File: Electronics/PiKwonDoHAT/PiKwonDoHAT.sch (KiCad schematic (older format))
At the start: 5 parts

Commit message: Finished HAT schematic
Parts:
- J1: renamed from J?; footprint (none) -> Pin_Headers:Pin_Header_Straight_2x20_Pitch2.54mm
- J2: renamed from J?; value RJ12-UNSHLD -> Judge3; footprint (none) -> PiKwonDo:TH-RJ12
- J3: renamed from J?; value RJ12-UNSHLD -> Judge2; footprint (none) -> PiKwonDo:TH-RJ12
- J4: renamed from J?; value RJ12-UNSHLD -> Judge1; footprint (none) -> PiKwonDo:TH-RJ12
- J5: renamed from J?; value RJ12-UNSHLD -> Controller; footprint (none) -> PiKwonDo:TH-RJ12
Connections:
- net labels added: CLK, LOAD
- net labels removed: VCC
- wire segments 0 -> 24
- no-connect marks 0 -> 41
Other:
- moved on the sheet: J1, J2, J3, J4, J5

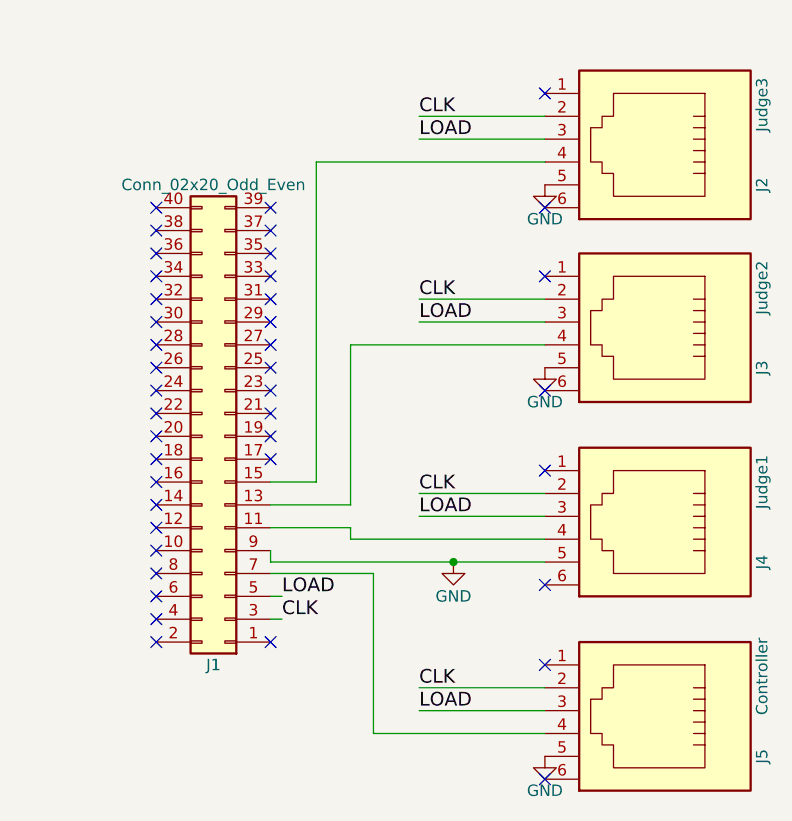
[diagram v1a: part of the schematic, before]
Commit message: Created HAT schematic and PCB
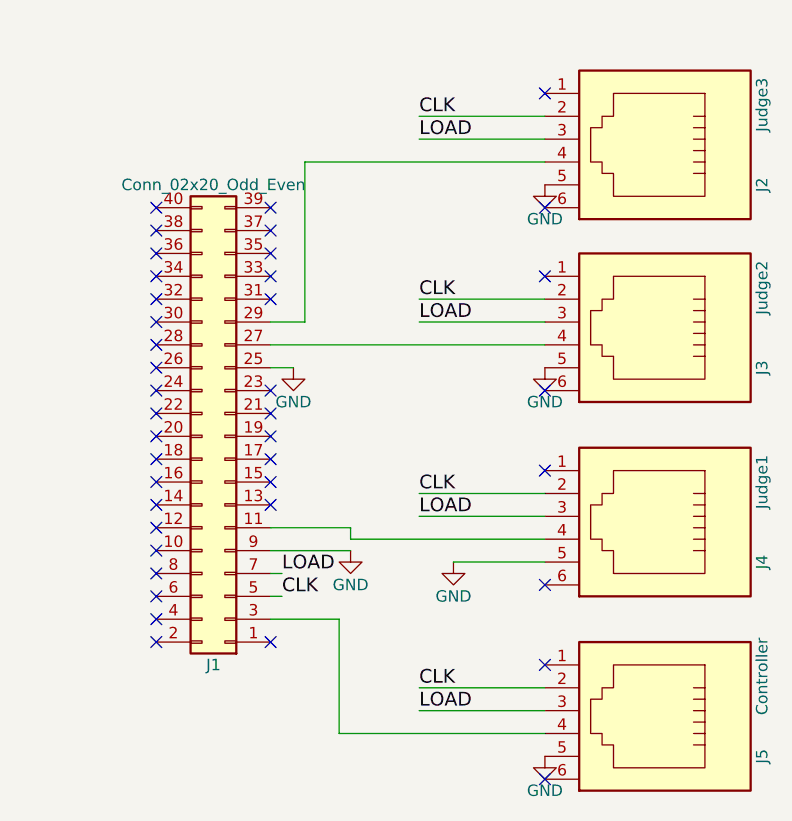
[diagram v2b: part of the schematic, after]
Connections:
- net CLK: now also J1.5 (Pin_5); no longer J1.3 (Pin_3)
- net GND: now also J1.25 (Pin_25)
- net LOAD: now also J1.7 (Pin_7); no longer J1.5 (Pin_5)
- net at J2.4: now also J1.29 (Pin_29); no longer J1.15 (Pin_15)
- net at J3.4: now also J1.27 (Pin_27); no longer J1.13 (Pin_13)
- net at J5.4: now also J1.3 (Pin_3); no longer J1.7 (Pin_7)
- no-connect marks 41 -> 40
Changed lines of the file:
@@
 LOAD
 Wire Wire Line
-	5800 3400 5850 3400
+	5800 3400 6100 3400
 Wire Wire Line
 	5800 3300 5850 3300
-Text Label 5850 3400 0    60   ~ 0
+Text Label 5850 3300 0    60   ~ 0
 CLK
-Text Label 5850 3300 0    60   ~ 0
+Text Label 5850 3200 0    60   ~ 0
 LOAD
-Wire Wire Line
-	7000 3900 6250 3900
-Wire Wire Line
-	6250 3900 6250 3200
-Wire Wire Line
-	6250 3200 5800 3200
 Wire Wire Line
 	7000 3050 6150 3050
@@
 	6150 3050 6150 3000
 Wire Wire Line
-	6150 3000 5800 3000
-Wire Wire Line
-	7000 2200 6150 2200
-Wire Wire Line
-	6150 2200 6150 2900
-Wire Wire Line
-	6150 2900 5800 2900
-Wire Wire Line
-	7000 1400 6000 1400
-Wire Wire Line
-	6000 1400 6000 2800
-Wire Wire Line
-	6000 2800 5800 2800
-Wire Wire Line
-	5800 3150 5800 3100
-Wire Wire Line
-	5800 3150 7000 3150
-Connection ~ 6600 3150
+	6600 3150 7000 3150
 NoConn ~ 5300 3500
 NoConn ~ 5300 3400
@@
 NoConn ~ 5300 1700
 NoConn ~ 5300 1600
-NoConn ~ 5800 3500
 NoConn ~ 5800 2700
 NoConn ~ 5800 2600
 NoConn ~ 5800 2500
 NoConn ~ 5800 2400
-NoConn ~ 5800 2300
-NoConn ~ 5800 2200
-NoConn ~ 5800 2100
 NoConn ~ 5800 2000
 NoConn ~ 5800 1900
@@
 NoConn ~ 5800 1700
 NoConn ~ 5800 1600
+Wire Wire Line
+	6150 3000 5800 3000
+Wire Wire Line
+	6100 3400 6100 3900
+Wire Wire Line
+	6100 3900 7000 3900
+Wire Wire Line
+	5800 3200 5850 3200
+NoConn ~ 5800 3500
+$Comp
+L GND #PWR07
+U 1 1 5B2B12EF
+P 6150 3100
+F 0 "#PWR07" H 6150 2850 50  0001 C CNN
+F 1 "GND" H 6150 2950 50  0000 C CNN
+F 2 "" H 6150 3100 50  0001 C CNN
+F 3 "" H 6150 3100 50  0001 C CNN
+	1    6150 3100
+	1    0    0    -1
+$EndComp
+Wire Wire Line
+	5800 3100 6150 3100
+$Comp
+L GND #PWR08
+U 1 1 5B2B134C
+P 5900 2300
+F 0 "#PWR08" H 5900 2050 50  0001 C CNN
+F 1 "GND" H 5900 2150 50  0000 C CNN
+F 2 "" H 5900 2300 50  0001 C CNN
+F 3 "" H 5900 2300 50  0001 C CNN
+	1    5900 2300
+	1    0    0    -1
+$EndComp
+Wire Wire Line
+	5800 2300 5900 2300
+NoConn ~ 5800 2800
+Wire Wire Line
+	7000 1400 5950 1400
+Wire Wire Line
+	5950 1400 5950 2100
+Wire Wire Line
+	5950 2100 5800 2100
+Wire Wire Line
+	5800 2200 7000 2200
+NoConn ~ 5800 2900
 $EndSCHEMATC

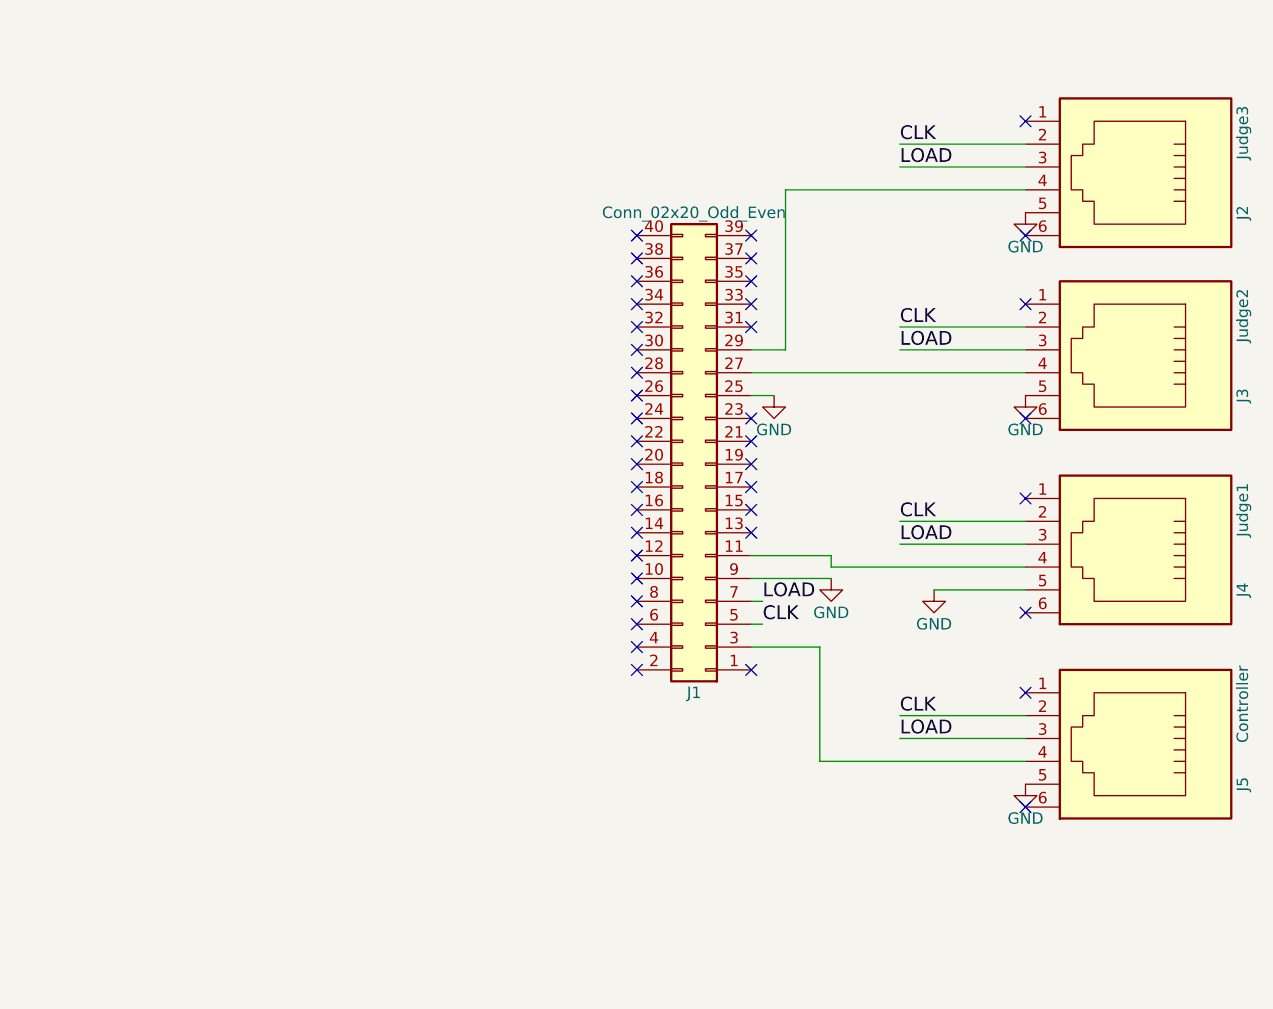
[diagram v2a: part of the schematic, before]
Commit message: Updated circuit protection elements to HAT schematic board.
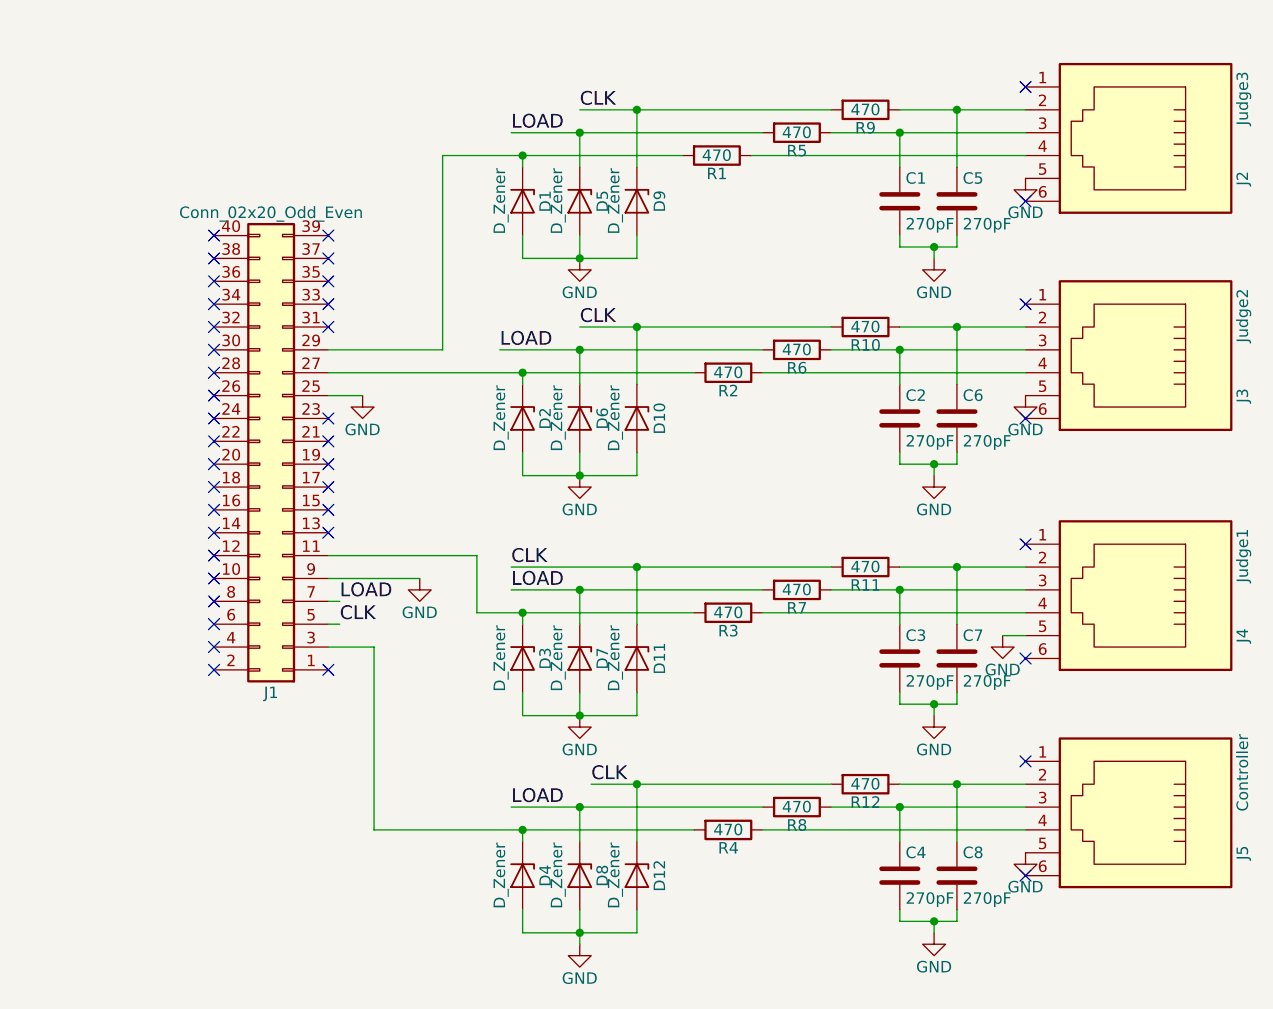
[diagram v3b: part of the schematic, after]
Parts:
- added C1, C2, C3, C4, C5, C6, C7, C8: 270pF, Capacitors_SMD:C_0603_HandSoldering, symbol C
- added D1, D10, D11, D12, D2, D3, D4, D5, D6, D7, D8, D9: D_Zener, Diodes_SMD:SOD-80C, symbol D_Zener
- added R1, R10, R11, R12, R2, R3, R4, R5, R6, R7, R8, R9: 470, Resistors_SMD:R_1206_HandSoldering, symbol R
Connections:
- net CLK: now also D10.1 (K), D11.1 (K), D12.1 (K), D9.1 (K), R10.2, R11.2, R12.2, R9.2; no longer J2.2, J3.2, J4.2, J5.2
- net GND: now also C1.2, C2.2, C3.2, C4.2, C5.2, C6.2, C7.2, C8.2, D1.2 (A), D10.2 (A), D11.2 (A), D12.2 (A), D2.2 (A), D3.2 (A), D4.2 (A), D5.2 (A), D6.2 (A), D7.2 (A), D8.2 (A), D9.2 (A)
- net LOAD: now also D5.1 (K), D6.1 (K), D7.1 (K), D8.1 (K), R5.2, R6.2, R7.2, R8.2; no longer J2.3, J3.3, J4.3, J5.3
- net at J2.4: now also R1.1; no longer J1.29 (Pin_29)
- net at J3.4: now also R2.1; no longer J1.27 (Pin_27)
- net at J4.4: now also R3.1; no longer J1.11 (Pin_11)
- net at J5.4: now also R4.1; no longer J1.3 (Pin_3)
- new net: C5.1, J2.2, R9.1
- new net: C1.1, J2.3, R5.1
- new net: C6.1, J3.2, R10.1
- new net: C2.1, J3.3, R6.1
- new net: C7.1, J4.2, R11.1
- new net: C3.1, J4.3, R7.1
- new net: C8.1, J5.2, R12.1
- new net: C4.1, J5.3, R8.1
- new net: D3.1 (K), J1.11 (Pin_11), R3.2
- new net: D2.1 (K), J1.27 (Pin_27), R2.2
- new net: D1.1 (K), J1.29 (Pin_29), R1.2
- new net: D4.1 (K), J1.3 (Pin_3), R4.2
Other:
- moved on the sheet: J1, J2, J4, J5

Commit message: Updated CAM files for Timer and PCB for HAT
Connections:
- net GND: now also J1.34 (Pin_34), J1.6 (Pin_6)
- no-connect marks 40 -> 38
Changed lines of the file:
@@
 LIBS:contrib
 LIBS:valves
-LIBS:Device
 LIBS:PiKwonDoHAT-cache
 EELAYER 25 0
@@
 NoConn ~ 3450 3500
 NoConn ~ 3450 3400
-NoConn ~ 3450 3300
 NoConn ~ 3450 3200
 NoConn ~ 3450 3100
@@
 NoConn ~ 3450 2100
 NoConn ~ 3450 2000
-NoConn ~ 3450 1900
 NoConn ~ 3450 1800
 NoConn ~ 3450 1700
@@
 Connection ~ 6450 3150
 Wire Wire Line
-	7000 4000 6450 4000
+	6450 4000 7000 4000
 Wire Wire Line
 	7000 4200 5850 4200
@@
 	4800 4250 4800 4200
 Connection ~ 4800 4200
+$Comp
+L GND #PWR?
+U 1 1 5B4F3E4D
+P 3300 3400
+F 0 "#PWR?" H 3300 3150 50  0001 C CNN
+F 1 "GND" H 3300 3250 50  0000 C CNN
+F 2 "" H 3300 3400 50  0001 C CNN
+F 3 "" H 3300 3400 50  0001 C CNN
+	1    3300 3400
+	1    0    0    -1
+$EndComp
+Wire Wire Line
+	3450 3300 3300 3300
+Wire Wire Line
+	3300 3300 3300 3400
+$Comp
+L GND #PWR?
+U 1 1 5B4F406A
+P 3250 2100
+F 0 "#PWR?" H 3250 1850 50  0001 C CNN
+F 1 "GND" H 3250 1950 50  0000 C CNN
+F 2 "" H 3250 2100 50  0001 C CNN
+F 3 "" H 3250 2100 50  0001 C CNN
+	1    3250 2100
+	1    0    0    -1
+$EndComp
+Wire Wire Line
+	3450 1900 3250 1900
+Wire Wire Line
+	3250 1900 3250 2100
 $EndSCHEMATC

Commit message: Finalized HAT PCB
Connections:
- net LOAD: now also J1.8 (Pin_8); no longer J1.7 (Pin_7)
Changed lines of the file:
@@
 LIBS:contrib
 LIBS:valves
+LIBS:Device
 LIBS:PiKwonDoHAT-cache
 EELAYER 25 0
@@
 Text Label 4000 3300 0    60   ~ 0
 CLK
-Text Label 4000 3200 0    60   ~ 0
+Text Label 3050 3200 0    60   ~ 0
 LOAD
 NoConn ~ 3450 3500
 NoConn ~ 3450 3400
-NoConn ~ 3450 3200
 NoConn ~ 3450 3100
 NoConn ~ 3450 3000
@@
 L GND #PWR08
 U 1 1 5B2B134C
-P 4100 2300
-F 0 "#PWR08" H 4100 2050 50  0001 C CNN
-F 1 "GND" H 4100 2150 50  0000 C CNN
-F 2 "" H 4100 2300 50  0001 C CNN
-F 3 "" H 4100 2300 50  0001 C CNN
-	1    4100 2300
+P 4350 2300
+F 0 "#PWR08" H 4350 2050 50  0001 C CNN
+F 1 "GND" H 4350 2150 50  0000 C CNN
+F 2 "" H 4350 2300 50  0001 C CNN
+F 3 "" H 4350 2300 50  0001 C CNN
+	1    4350 2300
 	1    0    0    -1
 $EndComp
@@
 	4150 3400 4150 4200
 Wire Wire Line
-	3950 3200 4000 3200
-Wire Wire Line
 	3950 3100 4350 3100
 Wire Wire Line
-	3950 2300 4100 2300
+	3950 2300 4350 2300
 Wire Wire Line
 	4450 1250 4450 2100
@@
 	4700 2100 5850 2100
 Wire Wire Line
-	3950 2200 5550 2200
-Wire Wire Line
 	5850 2200 7000 2200
 Connection ~ 6450 2100
@@
 Connection ~ 4800 4200
 $Comp
-L GND #PWR?
+L GND #PWR017
 U 1 1 5B4F3E4D
 P 3300 3400
-F 0 "#PWR?" H 3300 3150 50  0001 C CNN
+F 0 "#PWR017" H 3300 3150 50  0001 C CNN
 F 1 "GND" H 3300 3250 50  0000 C CNN
 F 2 "" H 3300 3400 50  0001 C CNN
@@
 	3300 3300 3300 3400
 $Comp
-L GND #PWR?
+L GND #PWR018
 U 1 1 5B4F406A
 P 3250 2100
-F 0 "#PWR?" H 3250 1850 50  0001 C CNN
+F 0 "#PWR018" H 3250 1850 50  0001 C CNN
 F 1 "GND" H 3250 1950 50  0000 C CNN
 F 2 "" H 3250 2100 50  0001 C CNN
@@
 Wire Wire Line
 	3250 1900 3250 2100
+Wire Wire Line
+	3950 2200 5550 2200
+NoConn ~ 3950 3200
+Wire Wire Line
+	3450 3200 3050 3200
 $EndSCHEMATC

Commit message: Added voltage buffer to HAT schematic
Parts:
- added C10, C11, C12, C9: 100pF, Capacitors_SMD:C_0805_HandSoldering, symbol C
- added U1, U2, U3, U4: 74LV1T34, TO_SOT_Packages_SMD:SOT-23-5_HandSoldering, symbol 74LV1T34
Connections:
- net CLK: now also U1.2 (A), U2.2 (A), U3.2 (A), U4.2 (A); no longer D10.1 (K), D11.1 (K), D12.1 (K), D9.1 (K), R10.2, R11.2, R12.2, R9.2
- net GND: now also C10.2, C11.2, C12.2, C9.2, U1.3 (GND), U2.3 (GND), U3.3 (GND), U4.3 (GND)
- net at D3.1 (K), J1.11 (Pin_11), R3.2: now also C11.1
- net at D2.1 (K), J1.27 (Pin_27), R2.2: now also C10.1
- net at D1.1 (K), J1.29 (Pin_29), R1.2: now also C9.1
- net at D4.1 (K), J1.3 (Pin_3), R4.2: now also C12.1
- net +5V: now reaches J1.37 (Pin_37)
- net +5V: now also J1.39 (Pin_39), U1.5 (VCC), U2.5 (VCC), U3.5 (VCC), U4.5 (VCC)
- new net: D9.1 (K), R9.2, U1.4 (Y)
- new net: D10.1 (K), R10.2, U4.4 (Y)
- new net: D11.1 (K), R11.2, U3.4 (Y)
- new net: D12.1 (K), R12.2, U2.4 (Y)
- no-connect marks 38 -> 36
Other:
- moved on the sheet: J1, R1, R5, R9
